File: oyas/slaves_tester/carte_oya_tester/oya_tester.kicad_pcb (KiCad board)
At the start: 2 copper layers, 99 x 99 mm, 55 parts, among them J1 Power, J2 Bus Oya, J6 Switches, SW3 Address, SW4 Select, U1 D148K, U2 MAX485E, U3 BPC_Alim5V, X2 Trou, X3 Trou, X4 Trou

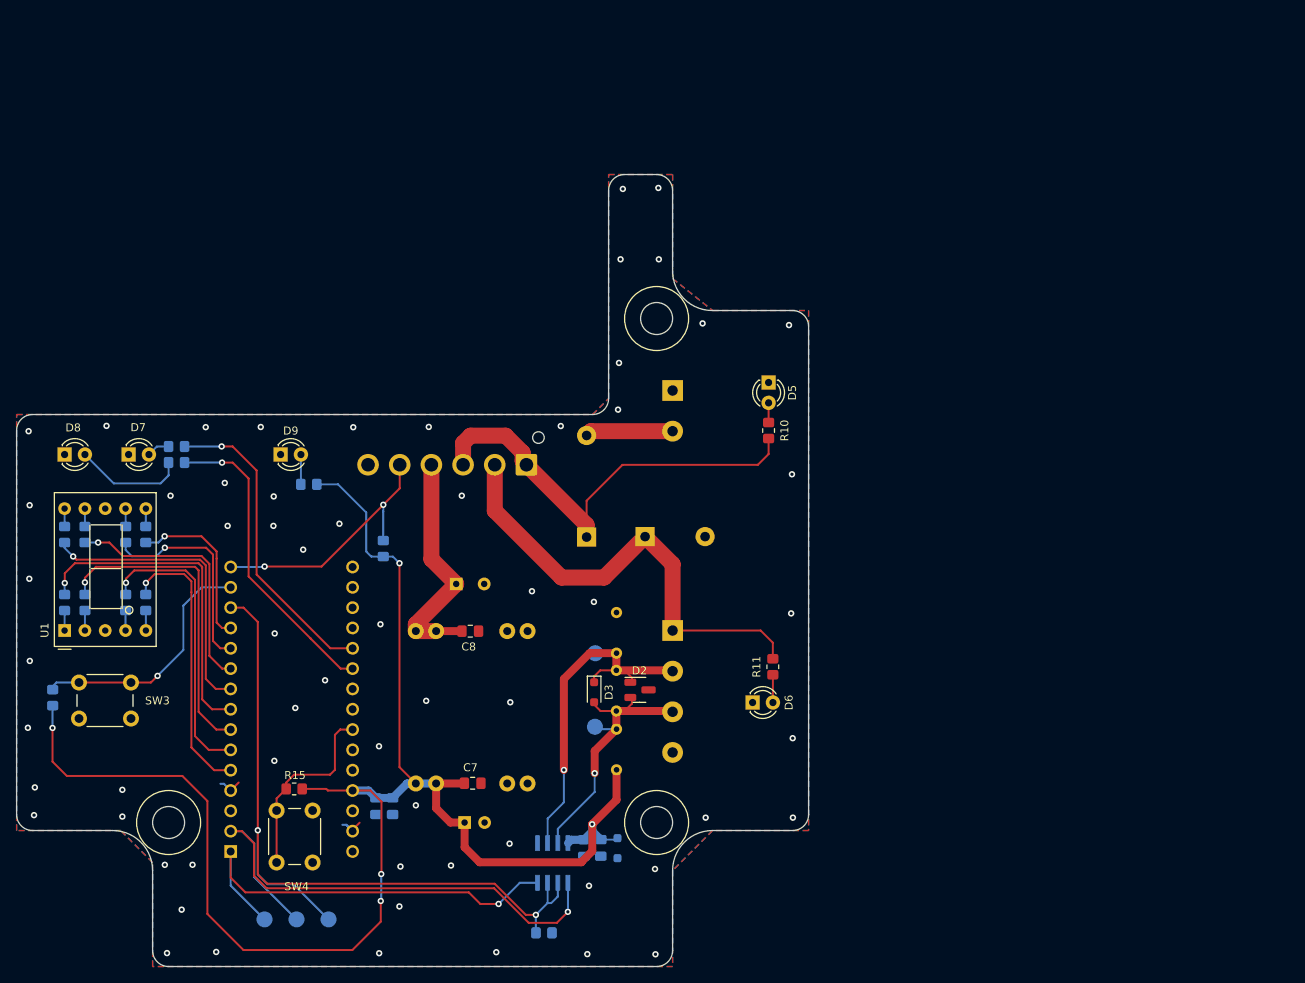
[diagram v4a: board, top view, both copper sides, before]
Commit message: Finalisation future Rev B
Ajout de protections sur le 12V Bus
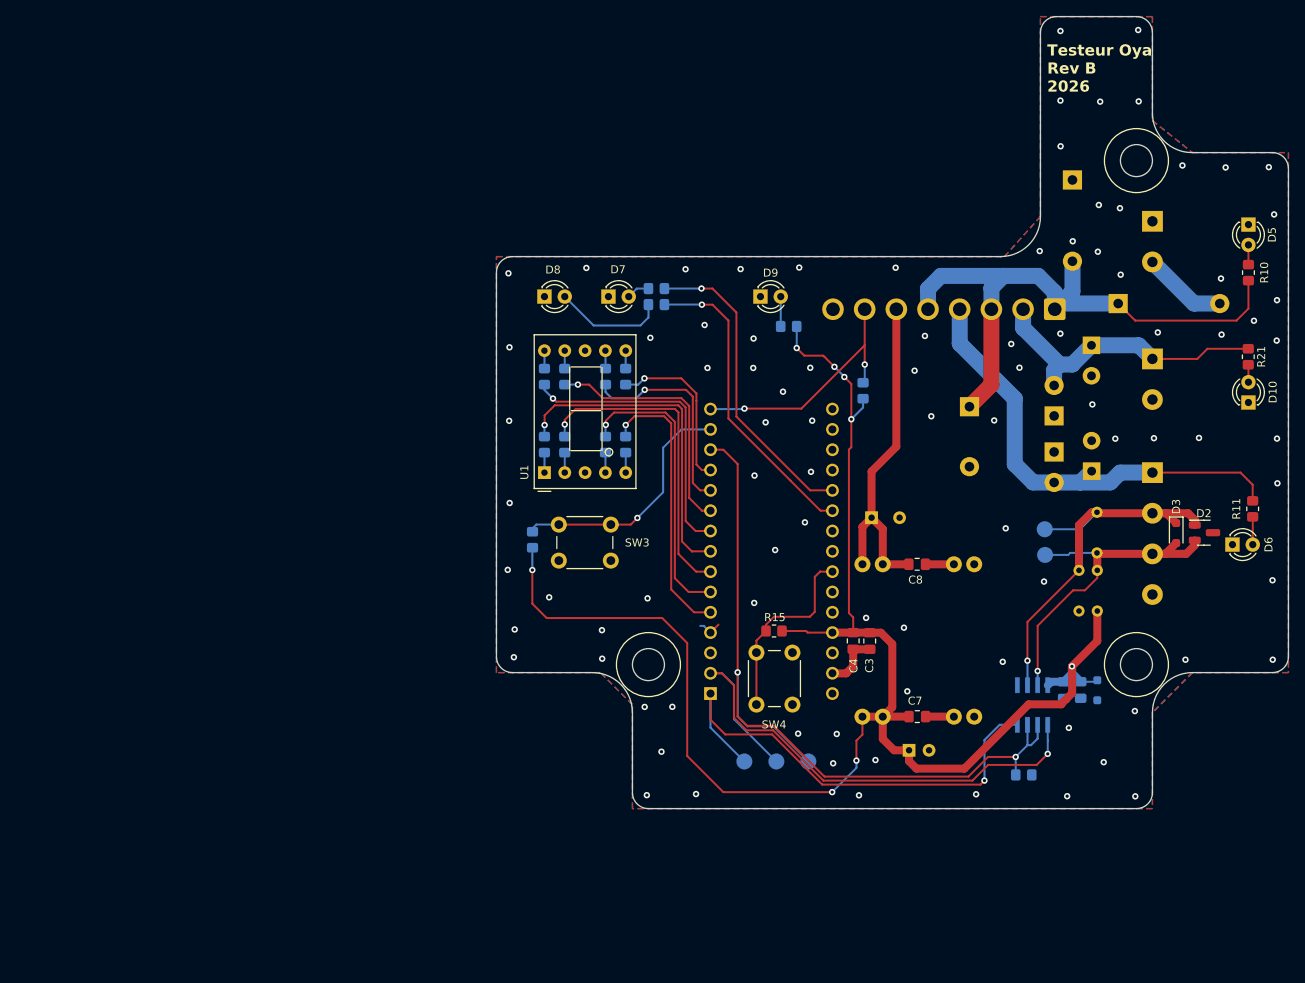
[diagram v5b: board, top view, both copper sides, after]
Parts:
- added D10: LED Rouge, LED_THT:LED_D3.0mm_FlatTop, F.Cu at (192.0, 91.5)
- added D11: 1N4007, Diode_THT:D_DO-41_SOD81_P3.81mm_Vertical_KathodeUp, B.Cu at (172.4, 84.3)
- added D12: P6KE16A, Diode_THT:D_DO-15_P3.81mm_Vertical_KathodeUp, B.Cu at (167.7, 93.2)
- added D13: P6KE16A, Diode_THT:D_DO-15_P10.16mm_Horizontal, B.Cu at (170.0, 63.7)
- added D14: 1N4007, Diode_THT:D_DO-41_SOD81_P3.81mm_Vertical_KathodeUp, B.Cu at (172.4, 100.1)
- added D15: P6KE16A, Diode_THT:D_DO-15_P3.81mm_Vertical_KathodeUp, B.Cu at (167.7, 97.7)
- added J3: EV, TerminalBlock_Phoenix:TerminalBlock_Phoenix_MKDS-1,5-2-5.08_1x02_P5.08mm_Horizontal, B.Cu at (180.0, 86.0)
- added R21: 1k, Resistor_SMD:R_0805_2012Metric_Pad1.20x1.40mm_HandSolder, F.Cu at (192.0, 85.8)
- C3, C4: moved to F.Cu
- J6: footprint Connector_JST:JST_VH_B6P-VH-FB-B_1x06_P3.96mm_Vertical -> Connector_JST:JST_VH_B8P-VH-B_1x08_P3.96mm_Vertical
- R18: value R -> 4.7k
- moved D3 75.4 mm to (182.9, 107.8)
- moved D2 73.2 mm to (186.4, 107.8)
- moved D4 72.6 mm to (175.7, 79.1), turned to 0 degrees
- moved J6 68.8 mm to (167.8, 79.8)
- moved J1 63.6 mm to (180.0, 68.8)
- moved R18 63.3 mm to (173.1, 117.6)
- moved R17 63.2 mm to (173.1, 110.3)
- moved D1 63.1 mm to (173.1, 127.5)
- moved D7 63.1 mm to (112.0, 78.3)
- moved D8 63.1 mm to (104.0, 78.3)
- moved R12 63.1 mm to (118.0, 77.3)
- moved R13 63.1 mm to (118.0, 79.3)
- moved R15 63.1 mm to (132.7, 120.1)
- moved R16 63.1 mm to (143.8, 90.0)
- moved R5 63.1 mm to (104.0, 96.8)
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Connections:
- C9 pad 1: SW_BUS -> POWER_12V
- J6 pad 2: SW_BUS -> SW_TST_EV
- J6 pad 4: SW_CPU -> SW_BUS
- J6 pad 5: ON_OFF -> POWER_12V
- J6 pad 6: GND -> SW_CPU
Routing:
- net SW_TST_EV: track 0.00 -> 37.5 mm
- net POWER_12V: track 56.9 -> 76.6 mm
- net SW_CPU: track 29.9 -> 43.3 mm
- net GND: track 7.26 -> 17.3 mm, vias 62 -> 90
- net BUS_B: track 36.2 -> 44.0 mm
- net TX: track 54.3 -> 61.3 mm
- net Net-(D10-A): track 0.00 -> 2.19 mm
- net TX_EN: track 99.6 -> 101.6 mm
- net BUS_A: track 48.1 -> 49.7 mm
- net RX: track 68.8 -> 70.4 mm
- net ON_OFF: track 32.6 -> 31.8 mm
- net +5V: track 202.1 -> 202.6 mm, vias 5 -> 8
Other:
- outline, holes or cut-outs redrawn
- board text added: "EV"
- board text added: "TST EV"
